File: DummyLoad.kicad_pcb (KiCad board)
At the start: 2 copper layers, 71 x 37 mm, 37 parts, among them J1 RF In, J2 RF Out

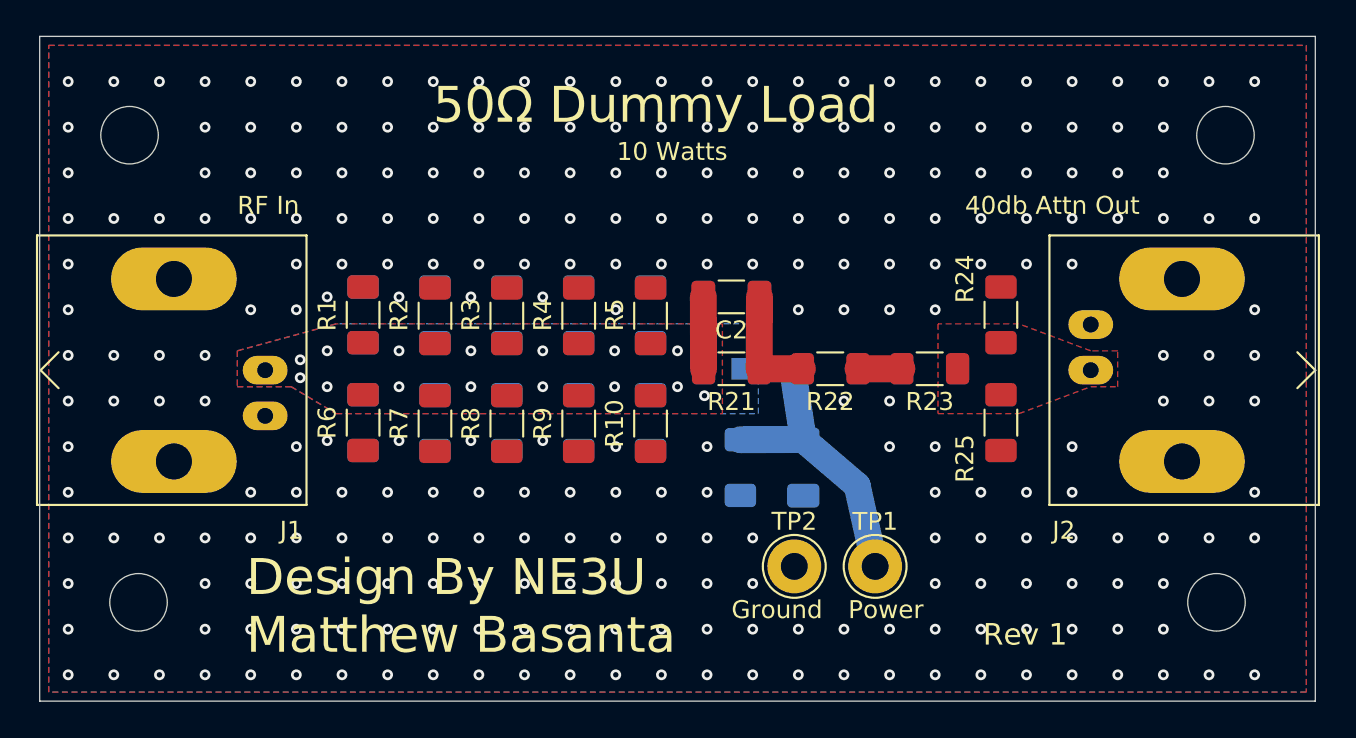
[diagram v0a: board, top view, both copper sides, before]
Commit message: Add TH testpoints and update PCB labels/layout
Add two through-hole testpoint footprints (RF In and GND) and reassign existing testpoint references (TP1/TP2 -> TP3/TP4). Adjusted testpoint coordinates and nets, updated multiple silkscreen texts (board name to "50Ω QRP Dummy Load", added designer credit, RF In/Ground labels) and repositioned several text items. Many via coordinates and UUIDs were updated to reflect the layout changes. These edits update the PCB to expose test points and tidy the board silk/placement for assembly and testing.
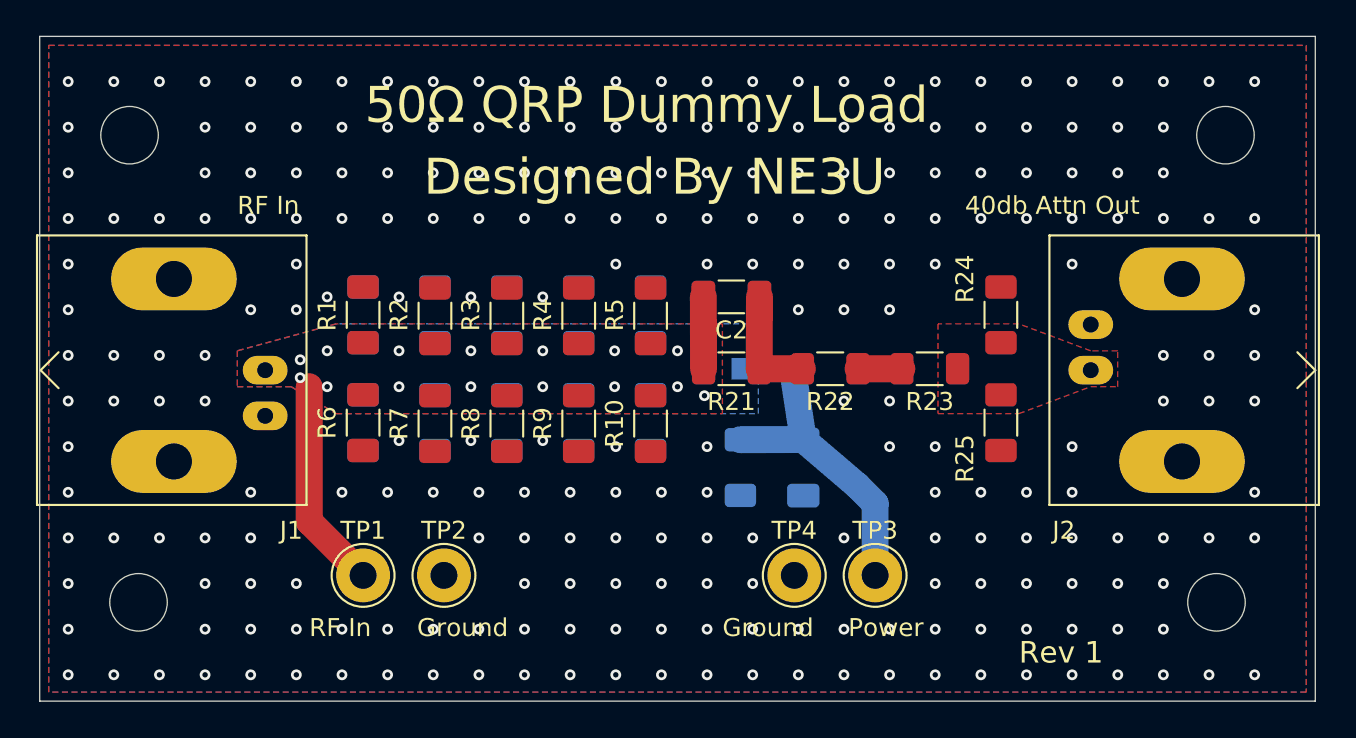
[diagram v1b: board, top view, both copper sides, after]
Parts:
- added TP1: RF In, TestPoint:TestPoint_THTPad_D3.0mm_Drill1.5mm, F.Cu at (116.5, 87.5)
- added TP2: GND, TestPoint:TestPoint_THTPad_D3.0mm_Drill1.5mm, F.Cu at (121.0, 87.5)
- moved TP3 0.50 mm to (145.0, 87.5)
- moved TP4 0.50 mm to (140.5, 87.5)
- renumbered TP1 to TP3, TP2 to TP4
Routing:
- net RF_In: track 4.00 -> 15.7 mm
- net Net-(D1-K): track 16.0 -> 16.8 mm
- net GND: vias 270 -> 249
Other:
- board text added: "50Ω QRP Dummy Load"
- board text added: "Designed By NE3U"
- board text removed: "10 Watts"
- board text removed: "50Ω Dummy Load"
- board text removed: "Design By NE3U Matthew Basanta"

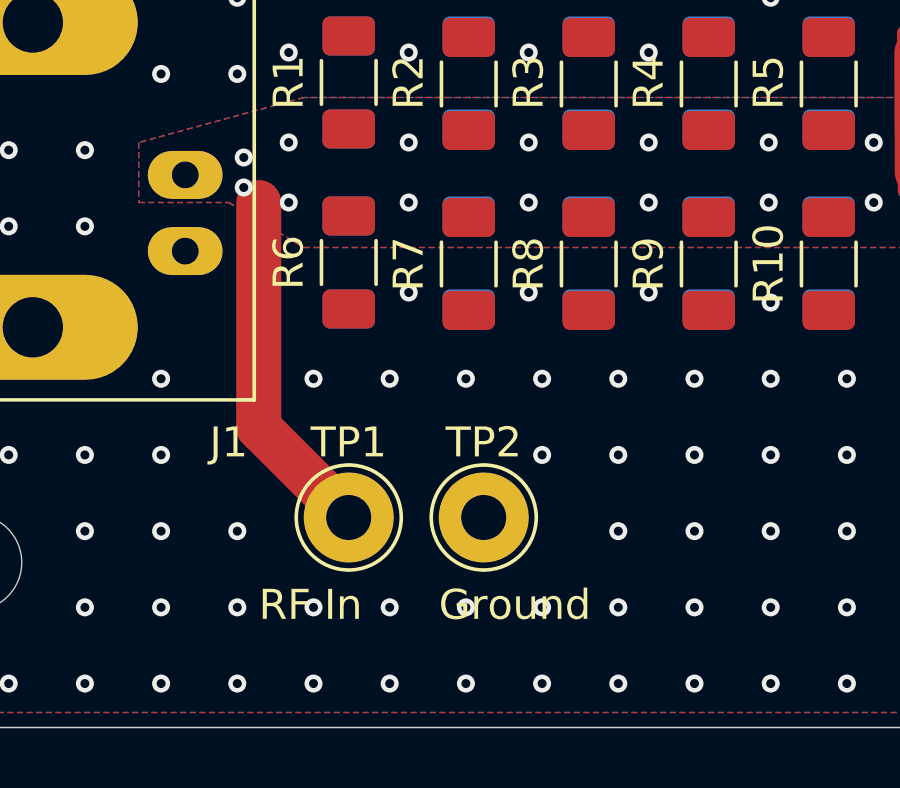
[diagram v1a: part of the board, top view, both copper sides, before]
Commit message: Adjust PCB testpoints, silks and via positions
Update DummyLoad.kicad_pcb: shift two THT testpoint footprints (TP1, TP2) and nudge silk labels ("RF In", "Ground"). Repositioned many vias across the board and regenerated their UUIDs to match the new coordinates. These edits realign component/text/via coordinates in the PCB layout; no schematic or netlist connectivity changes are indicated.
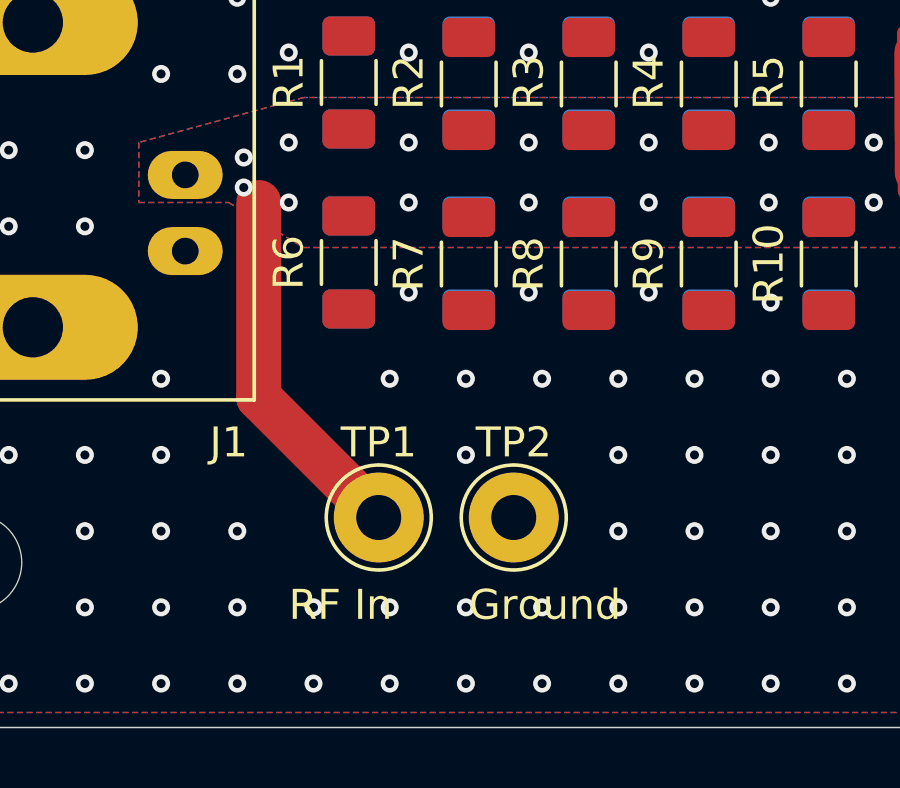
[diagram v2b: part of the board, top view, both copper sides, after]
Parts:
- moved TP1 1.00 mm to (117.5, 87.5)
- moved TP2 1.00 mm to (122.0, 87.5)
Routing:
- net GND: vias 249 -> 248
